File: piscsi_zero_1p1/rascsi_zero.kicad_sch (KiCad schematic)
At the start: 88 parts, among them J1 Raspberry_Pi_2_3, J4 I2C Pinout

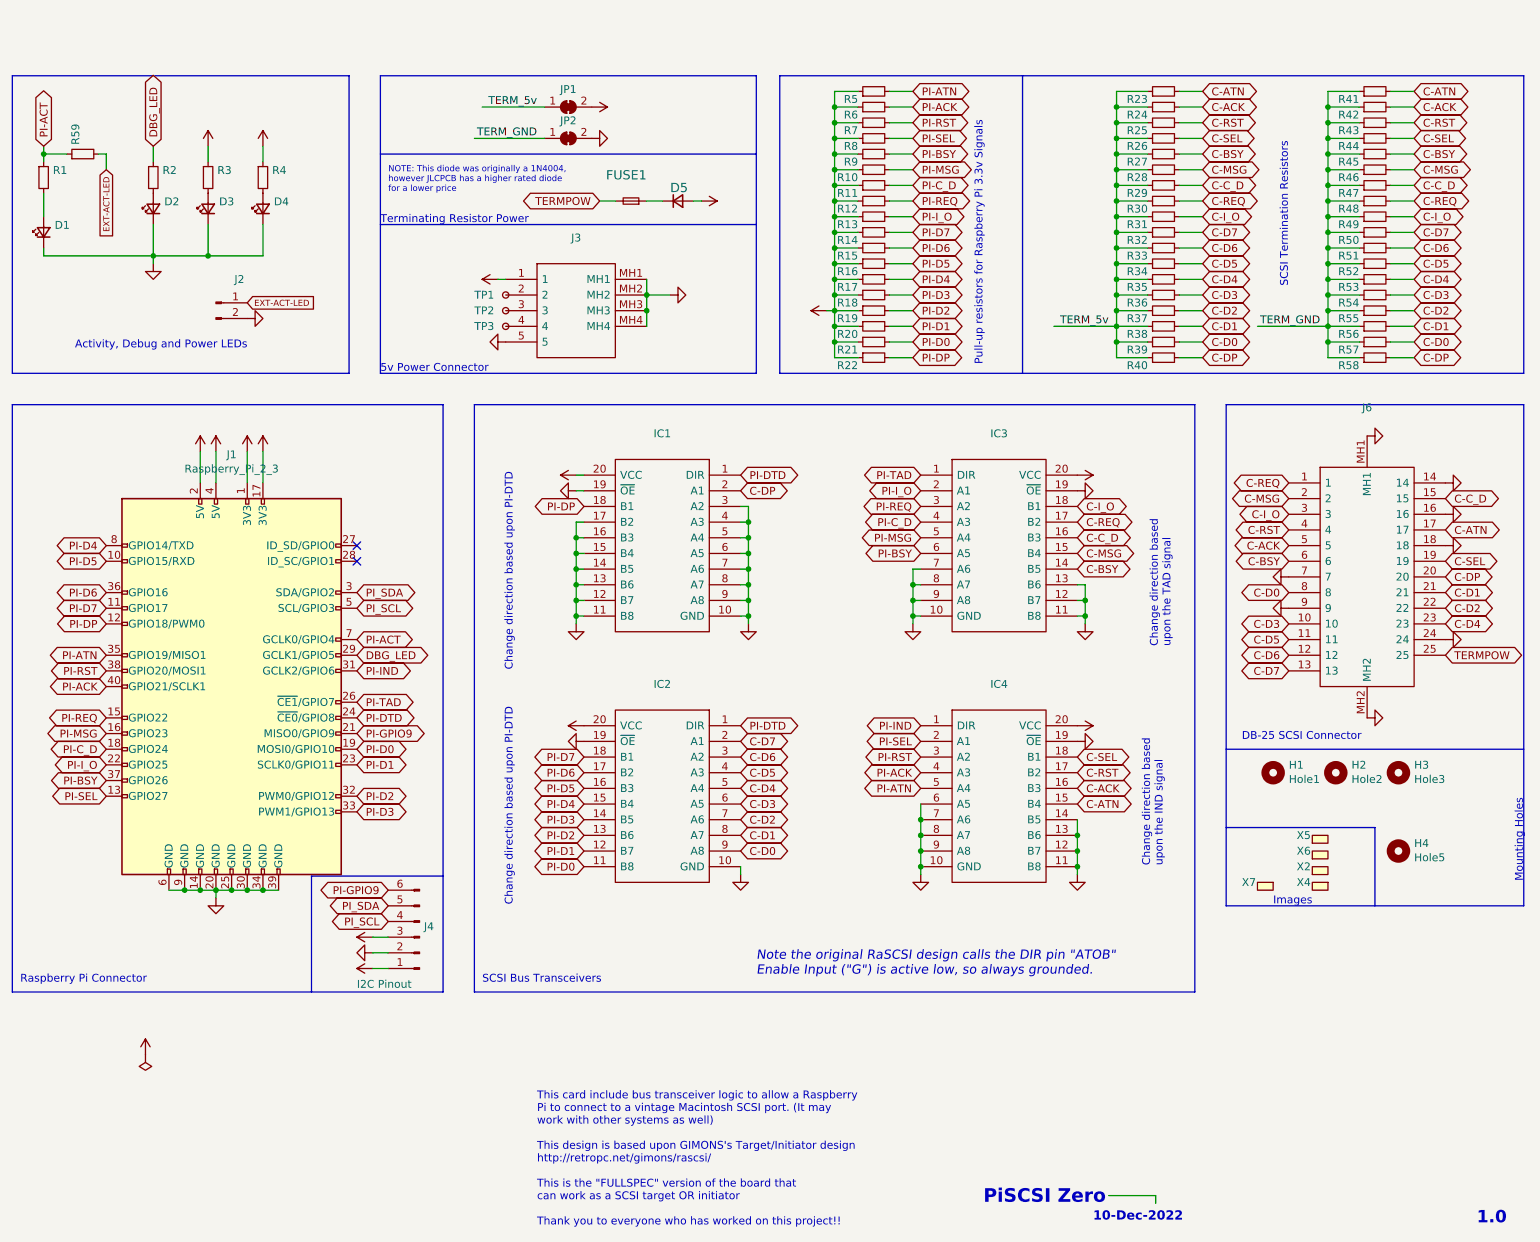
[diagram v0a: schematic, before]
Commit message: Updated to Kicad 7 & regenerate schematic
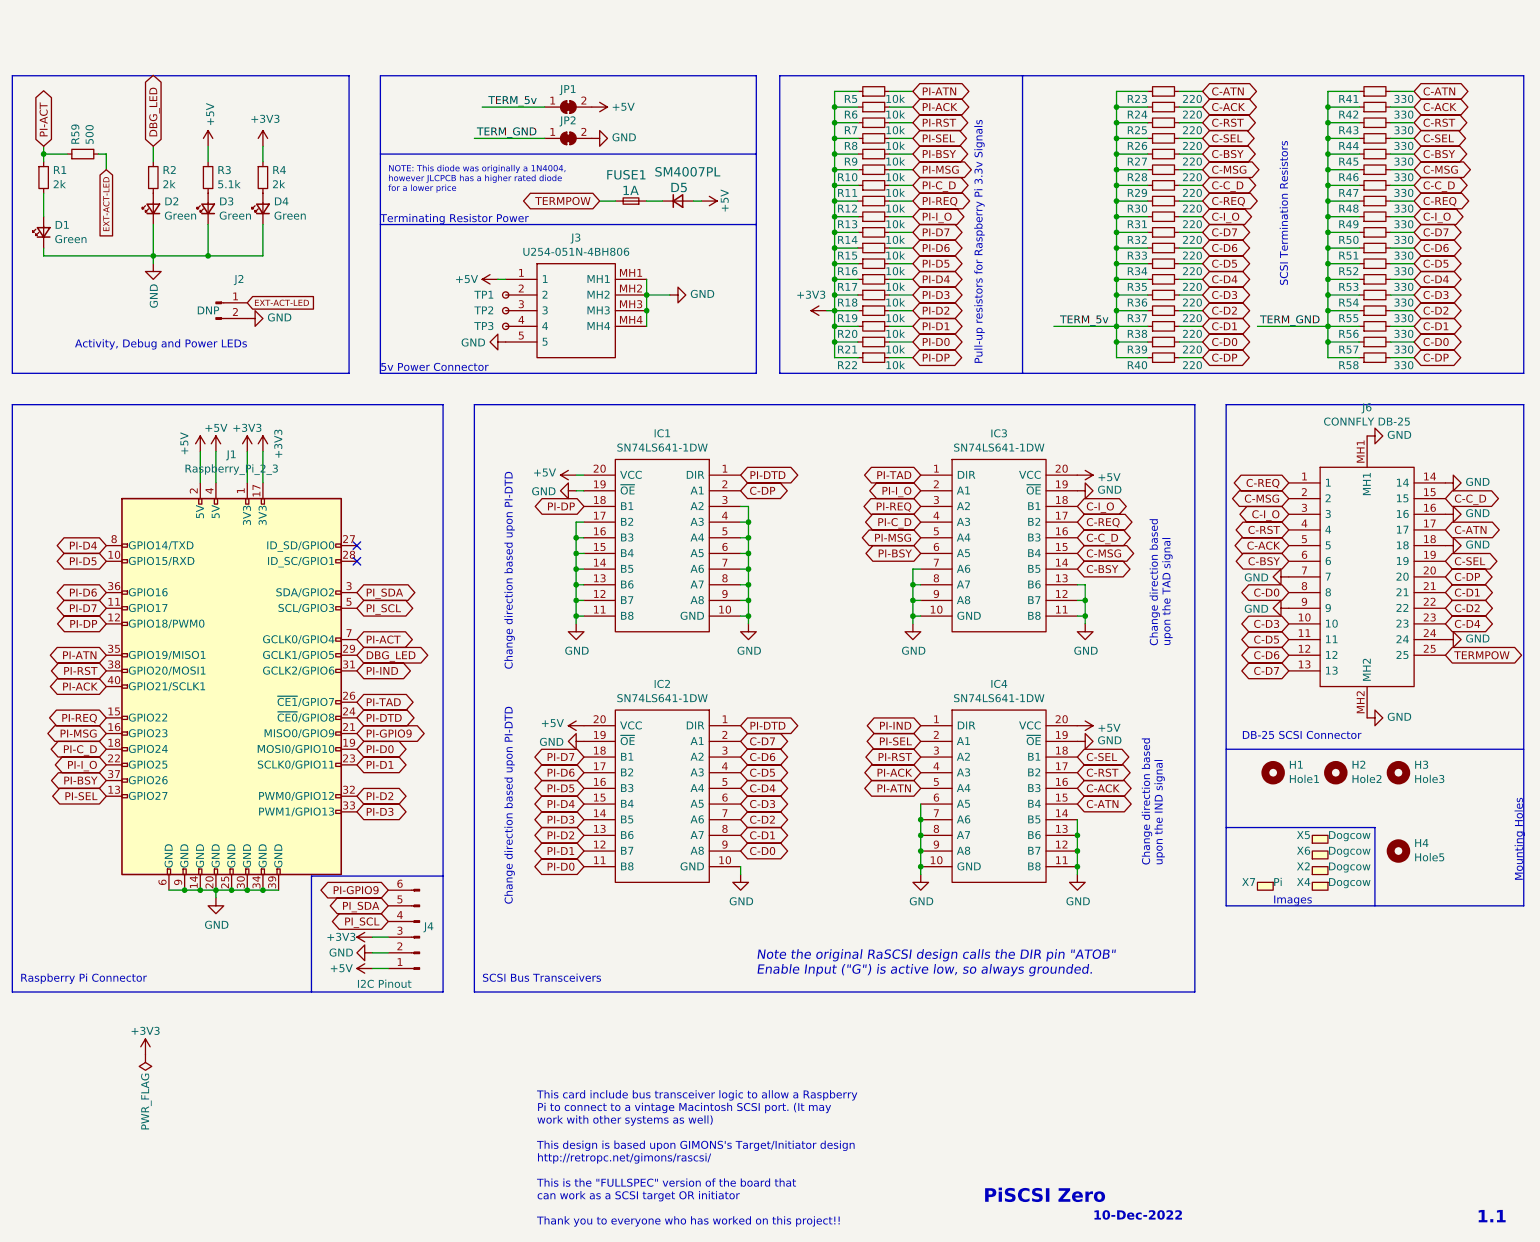
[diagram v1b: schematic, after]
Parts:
- D1, D2, D3, D4: value (none) -> Green
- D5: value (none) -> SM4007PL
- FUSE1: value (none) -> 1A
- IC1, IC2, IC3, IC4: value (none) -> SN74LS641-1DW
- J2: value (none) -> DNP
- J3: value (none) -> U254-051N-4BH806
- J6: value (none) -> CONNFLY DB-25
- JP1, JP2: value (none) -> SolderJumper_2_Bridged
- R1, R2, R4: value (none) -> 2k
- R10, R11, R12, R13, R14, R15, R16, R17, R18, R19, R20, R21, R22, R5, R6, R7, R8, R9: value (none) -> 10k
- R23, R24, R25, R26, R27, R28, R29, R30, R31, R32, R33, R34, R35, R36, R37, R38, R39, R40: value (none) -> 220
- R3: value (none) -> 5.1k
- R41, R42, R43, R44, R45, R46, R47, R48, R49, R50, R51, R52, R53, R54, R55, R56, R57, R58: value (none) -> 330
- R59: value (none) -> 500
- TP1, TP2, TP3: value (none) -> TestPoint_Small
- X2, X4, X5, X6: value (none) -> Dogcow
- X7: value (none) -> Pi
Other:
- note added: "1.1"
- note removed: "1.0"
